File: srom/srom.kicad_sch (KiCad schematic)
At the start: 12 parts, among them J1 Conn_01x03_Female, U1 4075, U2 74LS245, U3 74LS245, U4 74LS245, U5 Pico-rp2040

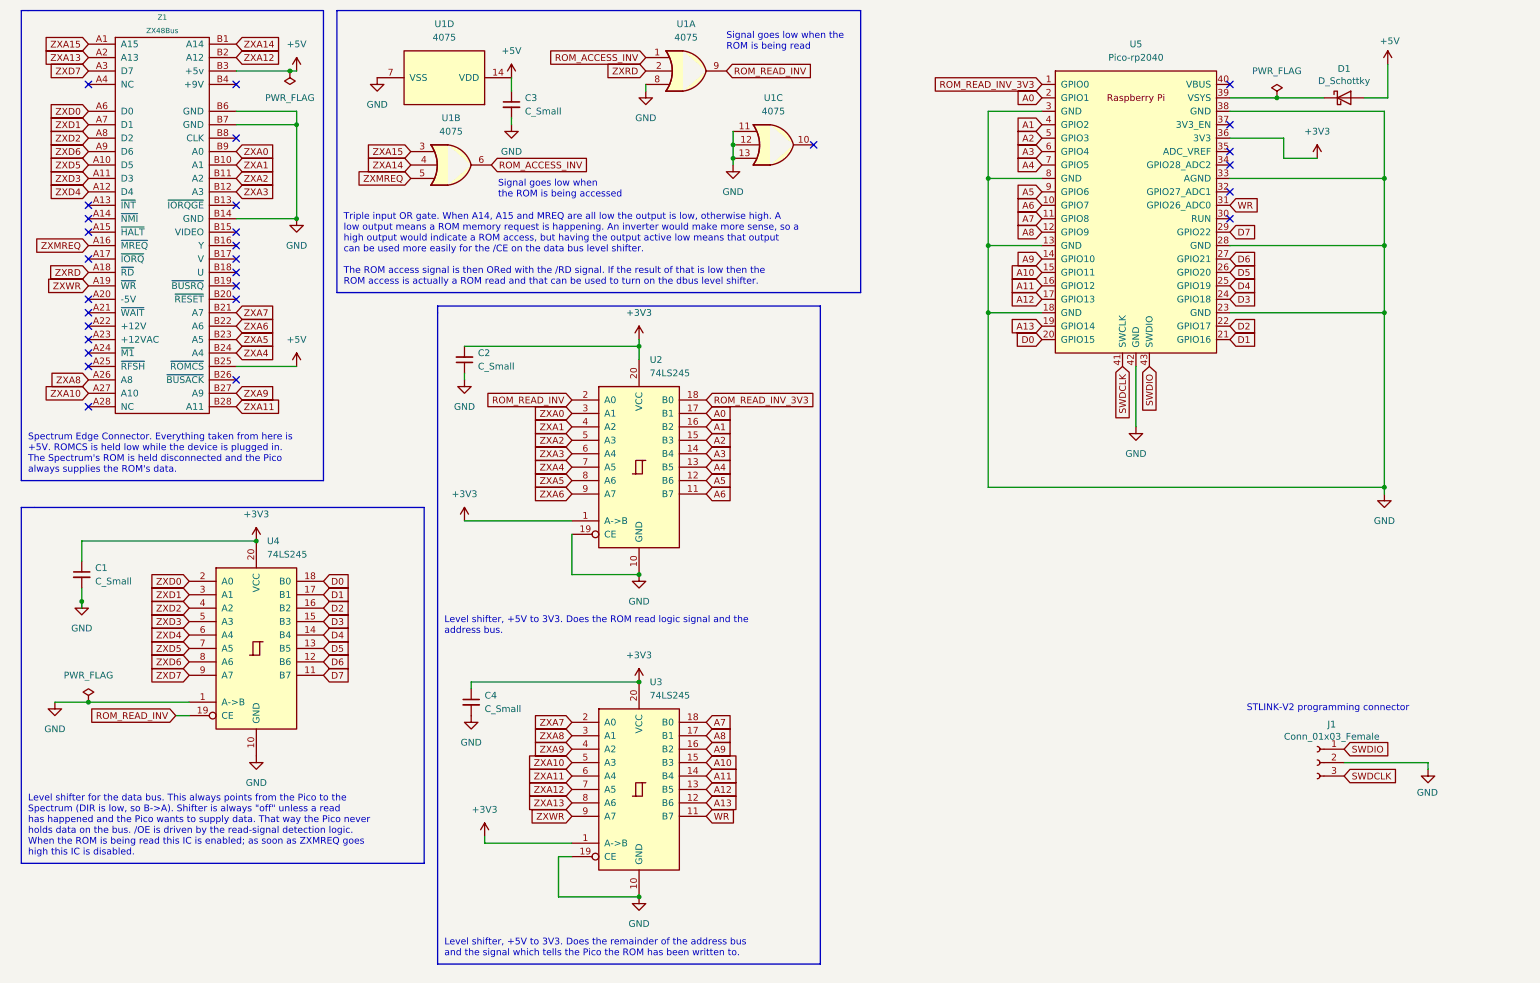
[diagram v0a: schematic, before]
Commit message: fix error on pico input, it needs to know about any access, not just reads
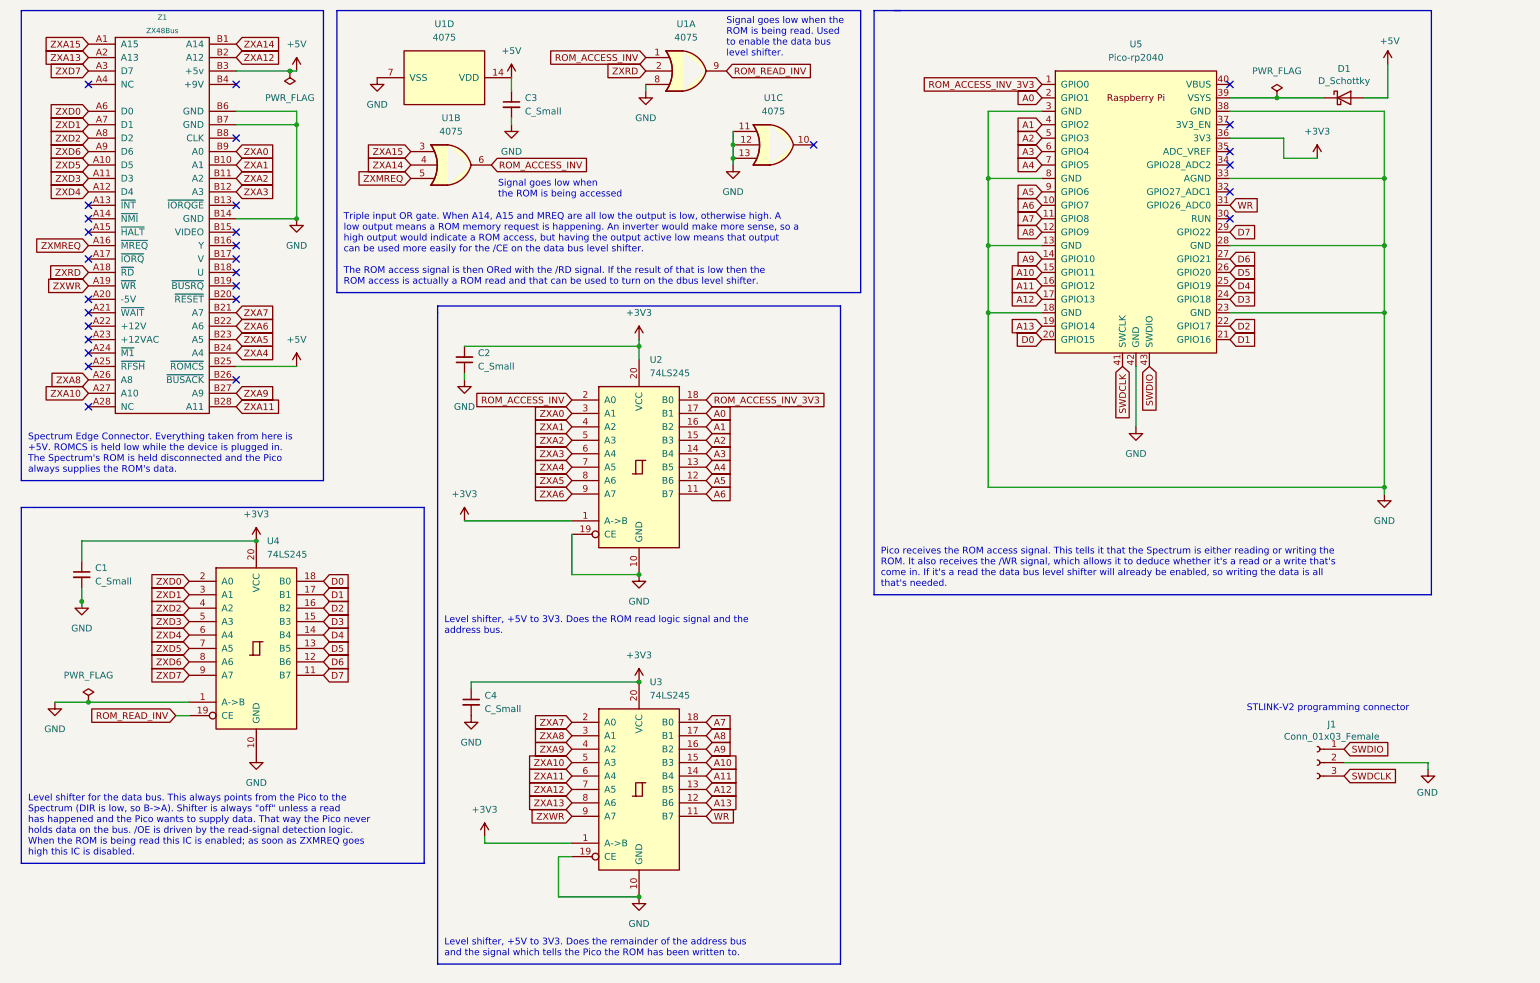
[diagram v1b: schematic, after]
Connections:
- net ROM_ACCESS_INV: now also U2.2 (A0)
- net ROM_READ_INV: no longer U2.2 (A0)
- net ROM_READ_INV_3V3 renamed ROM_ACCESS_INV_3V3
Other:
- note added: "Pico receives the ROM access signal. This tells it that the Spectrum is either reading or writing the ROM. It also receives the /WR signal, which allows it to deduce whether it's a read or a write that's come in. If it's a read the data bus level shifter will already be enabled, so writing the data is all that's needed."
- note added: "Signal goes low when the ROM is being read. Used to enable the data bus level shifter."
- note removed: "Signal goes low when the ROM is being read"
- title: (none) -> ZX Spectrum Pico ROM
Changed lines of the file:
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@@
 (kicad_sch (version 20211123) (generator eeschema)
   (paper "A4")
+  (title_block
+    (title "ZX Spectrum Pico ROM")
+    (date "2023-01-01")
+  )
   (junction (at 25.4 127) (diameter 0) (color 0 0 0 0)
   )
@@
     (stroke (width 0) (type default) (color 0 0 0 0))
   )
+  (polyline (pts (xy 175.26 125.73) (xy 175.26 15.24))
+    (stroke (width 0) (type default) (color 0 0 0 0))
+  )
   (wire (pts (xy 97.79 83.82) (xy 97.79 85.09))
     (stroke (width 0) (type default) (color 0 0 0 0))
@@
     (stroke (width 0) (type default) (color 0 0 0 0))
   )
+  (polyline (pts (xy 280.67 125.73) (xy 175.26 125.73))
+    (stroke (width 0) (type default) (color 0 0 0 0))
+  )
   (wire (pts (xy 272.415 25.4) (xy 272.415 31.75))
     (stroke (width 0) (type default) (color 0 0 0 0))
@@
     (stroke (width 0) (type default) (color 0 0 0 0))
   )
+  (polyline (pts (xy 280.67 15.24) (xy 280.67 125.73))
+    (stroke (width 0) (type default) (color 0 0 0 0))
+  )
   (wire (pts (xy 130.81 77.47) (xy 130.81 78.74))
     (stroke (width 0) (type default) (color 0 0 0 0))
@@
     (stroke (width 0) (type default) (color 0 0 0 0))
   )
-  (polyline (pts (xy 92.71 71.12) (xy 165.1 71.12))
+  (polyline (pts (xy 92.71 71.12) (xy 168.91 71.12))
     (stroke (width 0) (type default) (color 0 0 0 0))
   )
@@
     (stroke (width 0) (type default) (color 0 0 0 0))
   )
-  (polyline (pts (xy 165.1 71.12) (xy 165.1 195.58))
+  (polyline (pts (xy 168.91 71.12) (xy 168.91 195.58))
     (stroke (width 0) (type default) (color 0 0 0 0))
   )
@@
     (stroke (width 0) (type default) (color 0 0 0 0))
   )
+  (polyline (pts (xy 175.26 15.24) (xy 180.34 15.24))
+    (stroke (width 0) (type default) (color 0 0 0 0))
+  )
   (wire (pts (xy 25.4 124.46) (xy 25.4 127))
     (stroke (width 0) (type default) (color 0 0 0 0))
@@
     (stroke (width 0) (type default) (color 0 0 0 0))
   )
-  (polyline (pts (xy 165.1 195.58) (xy 92.71 195.58))
+  (polyline (pts (xy 168.91 195.58) (xy 92.71 195.58))
+    (stroke (width 0) (type default) (color 0 0 0 0))
+  )
+  (polyline (pts (xy 179.07 15.24) (xy 280.67 15.24))
     (stroke (width 0) (type default) (color 0 0 0 0))
   )
@@
     (effects (font (size 1.27 1.27)) (justify left bottom))
   )
+  (text "Pico receives the ROM access signal. This tells it that the Spectrum is either reading or writing the\nROM. It also receives the /WR signal, which allows it to deduce whether it's a read or a write that's\ncome in. If it's a read the data bus level shifter will already be enabled, so writing the data is all\nthat's needed."
+    (at 176.53 124.46 0)
+    (effects (font (size 1.27 1.27)) (justify left bottom))
+  )
   (text "Level shifter for the data bus. This always points from the Pico to the\nSpectrum (DIR is low, so B->A). Shifter is always \"off\" unless a read\nhas happened and the Pico wants to supply data. That way the Pico never\nholds data on the bus. /OE is driven by the read-signal detection logic.\nWhen the ROM is being read this IC is enabled; as soon as ZXMREQ goes\nhigh this IC is disabled."
     (at 15.24 175.26 0)
@@
     (effects (font (size 1.27 1.27)) (justify left bottom))
   )
-  (text "Signal goes low when the\nROM is being read" (at 147.32 22.86 0)
+  (text "Signal goes low when the\nROM is being read. Used\nto enable the data bus\nlevel shifter."
+    (at 147.32 24.13 0)
     (effects (font (size 1.27 1.27)) (justify left bottom))
   )
@@
     )
   )
-  (global_label "ROM_READ_INV_3V3" (shape input) (at 143.51 88.9 0) (fields_autoplaced)
-    (effects (font (size 1.27 1.27)) (justify left))
-    (property "Intersheet References" "${INTERSHEET_REFS}" (id 0) (at 164.1869 88.8206 0)
-      (effects (font (size 1.27 1.27)) (justify left) hide)
-    )
-  )
-  (global_label "ROM_READ_INV_3V3" (shape input) (at 207.01 29.21 180) (fields_autoplaced)
-    (effects (font (size 1.27 1.27)) (justify right))
-    (property "Intersheet References" "${INTERSHEET_REFS}" (id 0) (at 186.3331 29.1306 0)
+  (global_label "ROM_ACCESS_INV_3V3" (shape input) (at 143.51 88.9 0) (fields_autoplaced)
+    (effects (font (size 1.27 1.27)) (justify left))
+    (property "Intersheet References" "${INTERSHEET_REFS}" (id 0) (at 166.606 88.8206 0)
+      (effects (font (size 1.27 1.27)) (justify left) hide)
+    )
+  )
+  (global_label "ROM_ACCESS_INV_3V3" (shape input) (at 207.01 29.21 180) (fields_autoplaced)
+    (effects (font (size 1.27 1.27)) (justify right))
+    (property "Intersheet References" "${INTERSHEET_REFS}" (id 0) (at 183.914 29.1306 0)
       (effects (font (size 1.27 1.27)) (justify right) hide)
     )
@@
     )
   )
-  (global_label "ROM_READ_INV" (shape input) (at 118.11 88.9 180) (fields_autoplaced)
-    (effects (font (size 1.27 1.27)) (justify right))
-    (property "Intersheet References" "${INTERSHEET_REFS}" (id 0) (at 101.9083 88.8206 0)
-      (effects (font (size 1.27 1.27)) (justify right) hide)
-    )
+  (global_label "ROM_ACCESS_INV" (shape input) (at 118.11 88.9 180) (fields_autoplaced)
+    (effects (font (size 1.27 1.27)) (justify right))
+    (property "Intersheet References" "${INTERSHEET_REFS}" (id 0) (at 99.4893 88.8206 0)
+      (effects (font (size 1.27 1.27)) (justify right) hide)
+    )

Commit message: first effort at a layout
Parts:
- U1: footprint (none) -> Package_SO:SOIC-14_3.9x8.7mm_P1.27mm
- U2, U3, U4: footprint (none) -> Package_SO:SOIC-20W_7.5x12.8mm_P1.27mm
- U5: footprint RPi_Pico:RPi_Pico_SMD_TH -> pico-foot:RPi_Pico_SMD_TH; symbol rp-pico:Pico-rp2040 -> pico-sym:Pico
- Z1: footprint (none) -> zxbus:ZX_Bus_Pin_Header
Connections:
- net A0: now also U2.15 (B3), U5.15 (GPIO11); no longer U2.17 (B1), U5.2 (GPIO1)
- net A1: now also U2.14 (B4), U5.16 (GPIO12); no longer U2.16 (B2), U5.4 (GPIO2)
- net A10: now also U3.12 (B6), U5.22 (GPIO17); no longer U3.15 (B3), U5.15 (GPIO11)
- net A11: now also U3.11 (B7), U5.21 (GPIO16); no longer U3.14 (B4), U5.16 (GPIO12)
- net A12: now also U2.16 (B2), U5.14 (GPIO10); no longer U3.13 (B5), U5.17 (GPIO13)
- net A13: now also U2.17 (B1), U5.12 (GPIO9); no longer U3.12 (B6), U5.19 (GPIO14)
- net A2: now also U2.13 (B5), U5.17 (GPIO13); no longer U2.15 (B3), U5.5 (GPIO3)
- net A3: now also U2.12 (B6), U5.19 (GPIO14); no longer U2.14 (B4), U5.6 (GPIO4)
- net A4: now also U3.15 (B3), U5.26 (GPIO20); no longer U2.13 (B5), U5.7 (GPIO5)
- net A5: now also U3.16 (B2), U5.27 (GPIO21); no longer U2.12 (B6), U5.9 (GPIO6)
- net A6: now also U3.17 (B1), U5.29 (GPIO22); no longer U2.11 (B7), U5.10 (GPIO7)
- net A7: now also U5.31 (GPIO26_ADC0); no longer U5.11 (GPIO8)
- net A8: now also U3.14 (B4), U5.25 (GPIO19); no longer U3.17 (B1), U5.12 (GPIO9)
- net A9: now also U3.13 (B5), U5.24 (GPIO18); no longer U3.16 (B2), U5.14 (GPIO10)
- net D0: now also U5.1 (GPIO0); no longer U5.20 (GPIO15)
- net D1: now also U5.2 (GPIO1); no longer U5.21 (GPIO16)
- net D2: now also U5.4 (GPIO2); no longer U5.22 (GPIO17)
- net D3: now also U4.14 (B4), U5.6 (GPIO4); no longer U4.15 (B3), U5.24 (GPIO18)
- net D4: now also U4.12 (B6), U5.9 (GPIO6); no longer U4.14 (B4), U5.25 (GPIO19)
- net D5: now also U4.15 (B3), U5.5 (GPIO3); no longer U4.13 (B5), U5.26 (GPIO20)
- net D6: now also U4.13 (B5), U5.7 (GPIO5); no longer U4.12 (B6), U5.27 (GPIO21)
- net D7: now also U5.10 (GPIO7); no longer U5.29 (GPIO22)
- net ROM_ACCESS_INV_3V3: now also U5.11 (GPIO8); no longer U5.1 (GPIO0)
- net WR: now also U2.11 (B7), U5.20 (GPIO15); no longer U3.11 (B7), U5.31 (GPIO26_ADC0)
- net ZXA0: now also U2.5 (A3); no longer U2.3 (A1)
- net ZXA1: now also U2.6 (A4); no longer U2.4 (A2)
- net ZXA10: now also U3.8 (A6); no longer U3.5 (A3)
- net ZXA11: now also U3.9 (A7); no longer U3.6 (A4)
- net ZXA12: now also U2.4 (A2); no longer U3.7 (A5)
- net ZXA13: now also U2.3 (A1); no longer U3.8 (A6)
- net ZXA2: now also U2.7 (A5); no longer U2.5 (A3)
- net ZXA3: now also U2.8 (A6); no longer U2.6 (A4)
- net ZXA4: now also U3.5 (A3); no longer U2.7 (A5)
- net ZXA5: now also U3.4 (A2); no longer U2.8 (A6)
- net ZXA6: now also U3.3 (A1); no longer U2.9 (A7)
- net ZXA8: now also U3.6 (A4); no longer U3.3 (A1)
- net ZXA9: now also U3.7 (A5); no longer U3.4 (A2)
- net ZXD3: now also U4.6 (A4); no longer U4.5 (A3)
- net ZXD4: now also U4.8 (A6); no longer U4.6 (A4)
- net ZXD5: now also U4.5 (A3); no longer U4.7 (A5)
- net ZXD6: now also U4.7 (A5); no longer U4.8 (A6)
- net ZXWR: now also U2.9 (A7); no longer U3.9 (A7)

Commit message: fix a couple of footprint errors with v1.0
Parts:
- D1: footprint Diode_SMD:D_SOD-323_HandSoldering -> Diode_SMD:D_1206_3216Metric_Pad1.42x1.75mm_HandSolder
- U2, U3, U4: footprint Package_SO:SOIC-20W_7.5x12.8mm_P1.27mm -> Package_SO:SO-20_5.3x12.6mm_P1.27mm
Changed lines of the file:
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@@
   (title_block
     (title "ZX Spectrum Pico ROM")
-    (date "2023-01-01")
+    (date "2023-01-18")
+    (rev "1.1")
   )
   (junction (at 25.4 127) (diameter 0) (color 0 0 0 0)
@@
       (effects (font (size 1.27 1.27)) (justify left))
     )
-    (property "Footprint" "Package_SO:SOIC-20W_7.5x12.8mm_P1.27mm" (id 2) (at 58.42 135.89 0)
+    (property "Footprint" "Package_SO:SO-20_5.3x12.6mm_P1.27mm" (id 2) (at 58.42 135.89 0)
       (effects (font (size 1.27 1.27)) hide)
     )
@@
       (effects (font (size 1.27 1.27)) (justify left))
     )
-    (property "Footprint" "Package_SO:SOIC-20W_7.5x12.8mm_P1.27mm" (id 2) (at 130.81 101.6 0)
+    (property "Footprint" "Package_SO:SO-20_5.3x12.6mm_P1.27mm" (id 2) (at 130.81 101.6 0)
       (effects (font (size 1.27 1.27)) hide)
     )
@@
       (effects (font (size 1.27 1.27)) (justify left))
     )
-    (property "Footprint" "Package_SO:SOIC-20W_7.5x12.8mm_P1.27mm" (id 2) (at 130.81 162.56 0)
+    (property "Footprint" "Package_SO:SO-20_5.3x12.6mm_P1.27mm" (id 2) (at 130.81 162.56 0)
       (effects (font (size 1.27 1.27)) hide)
     )
@@
     (property "Reference" "D1" (id 0) (at 264.16 26.2382 0))
     (property "Value" "D_Schottky" (id 1) (at 264.16 28.5496 0))
-    (property "Footprint" "Diode_SMD:D_SOD-323_HandSoldering" (id 2) (at 264.16 31.75 0)
+    (property "Footprint" "Diode_SMD:D_1206_3216Metric_Pad1.42x1.75mm_HandSolder" (id 2) (at 264.16 31.75 0)
       (effects (font (size 1.27 1.27)) hide)
     )
@@
     )
     (path "/986f0686-4dd2-4d11-a20b-857347ffd112"
-      (reference "D1") (unit 1) (value "D_Schottky") (footprint "Diode_SMD:D_SOD-323_HandSoldering")
+      (reference "D1") (unit 1) (value "D_Schottky") (footprint "Diode_SMD:D_1206_3216Metric_Pad1.42x1.75mm_HandSolder")
     )
     (path "/f1c41838-eb1e-47a4-8dba-8e7e84008063"
@@
     )
     (path "/50f1c47b-dcfb-48bb-ab30-5deb35a88ec4"
-      (reference "U2") (unit 1) (value "74LS245") (footprint "Package_SO:SOIC-20W_7.5x12.8mm_P1.27mm")
+      (reference "U2") (unit 1) (value "74LS245") (footprint "Package_SO:SO-20_5.3x12.6mm_P1.27mm")
     )
     (path "/5e3e627e-19b1-4d8a-8392-17f9e86892e1"
-      (reference "U3") (unit 1) (value "74LS245") (footprint "Package_SO:SOIC-20W_7.5x12.8mm_P1.27mm")
+      (reference "U3") (unit 1) (value "74LS245") (footprint "Package_SO:SO-20_5.3x12.6mm_P1.27mm")
     )
     (path "/0d903a43-d7cf-4289-a942-f915aaae1c46"
-      (reference "U4") (unit 1) (value "74LS245") (footprint "Package_SO:SOIC-20W_7.5x12.8mm_P1.27mm")
+      (reference "U4") (unit 1) (value "74LS245") (footprint "Package_SO:SO-20_5.3x12.6mm_P1.27mm")
     )
     (path "/e821345b-c1ac-4e84-af10-b11a34f6e4b2"
